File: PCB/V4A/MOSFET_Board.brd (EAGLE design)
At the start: 230 x 120 mm, 227 parts, among them IC1 7805T, IC2 7805T, Q101 SIRC10DP, Q102 SIRC10DP, Q103 BC817, Q104 BC817, Q105 SIRC10DP, Q106 SIRC10DP, Q107 BC817, Q108 BC807, Q109 BC817, Q110 BC807, Q111 IXTK102N65X2, Q112 IXTK102N65X2, Q301 BC807, Q302 BC807, Q303 BC807, Q304 BC807, Q305 BC807, Q306 BC807, Q307 BC807, Q308 BC807, U1 LM50, U101 AD420, U102 AD420, U103 LT1014I, U104 LT1014I, U105 AD620, U106 AD620, U107 AD620, U108 AD620, U109 LTC1865L, U110 LTC1865L, U111 LP2985-3.1, U2 LM50, U205 AD620, U208 LTC1865L, U3 LTC1865L, U301 HCPL-063N, U302 HCPL-063N, U303 HCPL-063N, U304 HCPL-063N, U4 MAX743, X1 GMSTBA4

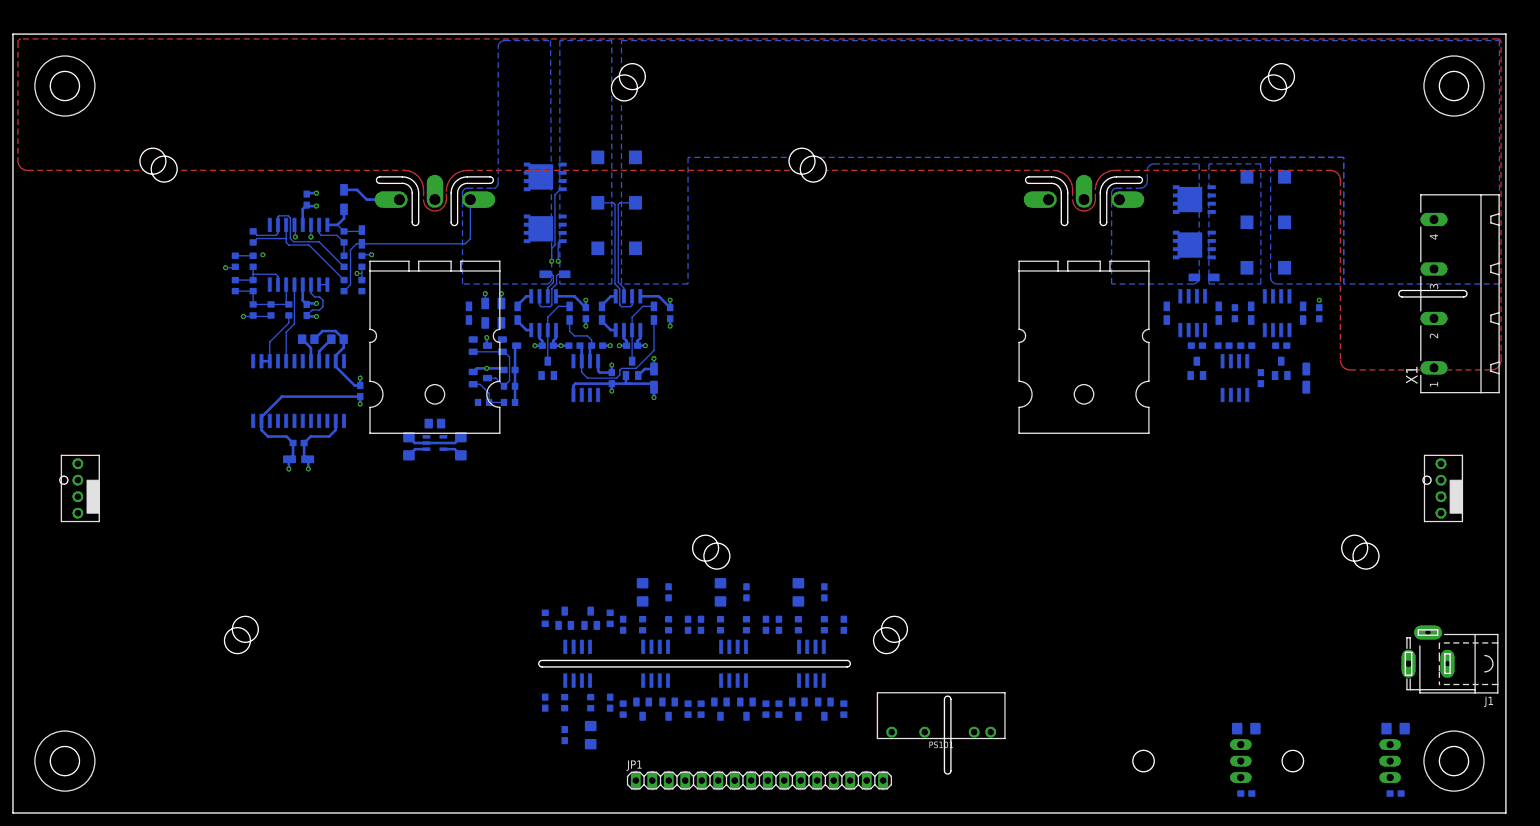
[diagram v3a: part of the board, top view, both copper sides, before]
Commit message: Added block diagram
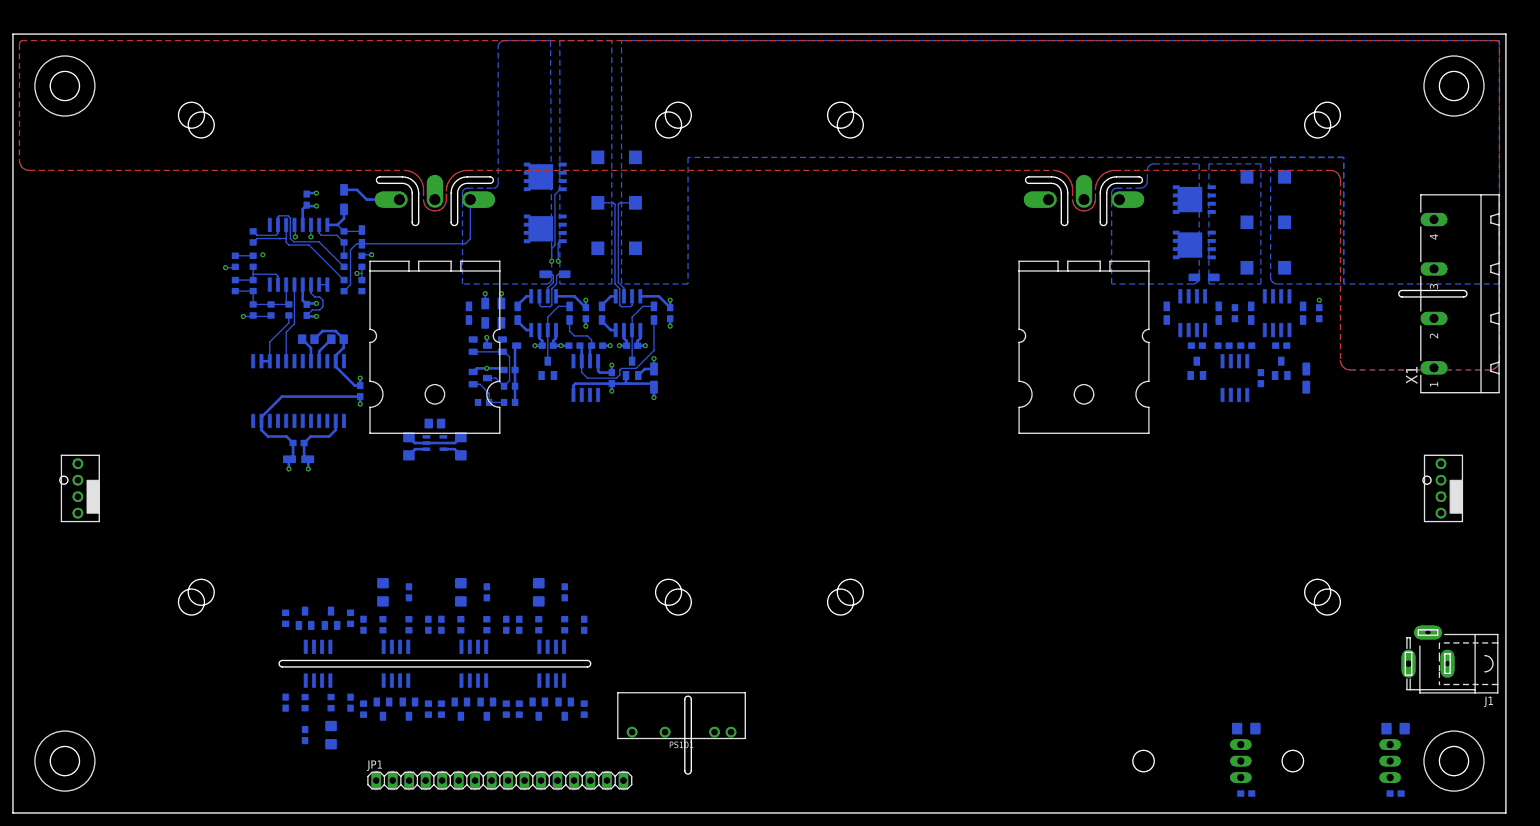
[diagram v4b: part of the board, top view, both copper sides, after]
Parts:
- moved C301 40.0 mm to (-54.0, -36.0)
- moved C302 40.0 mm to (-30.0, -36.0)
- moved C303 40.0 mm to (-58.0, -36.0)
- moved C304 40.0 mm to (-34.0, -36.0)
- moved C305 40.0 mm to (-51.0, -41.0)
- moved C306 40.0 mm to (-27.0, -41.0)
- moved C307 40.0 mm to (-61.0, -41.0)
- moved C308 40.0 mm to (-37.0, -41.0)
- moved C309 40.0 mm to (-42.0, -36.0)
- moved C310 40.0 mm to (-70.0, -58.0)
- moved C311 40.0 mm to (-46.0, -36.0)
- moved C312 40.0 mm to (-66.0, -58.0)
- moved C313 40.0 mm to (-39.0, -41.0)
- moved C314 40.0 mm to (-49.0, -41.0)
- moved C315 40.0 mm to (-73.0, -53.0)
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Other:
- outline, holes or cut-outs redrawn

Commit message: PCB layout, cleaned part list
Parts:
- removed C1, C11, C110, C3, C6: 1µ, passives:CT3216
- removed C10: 10µ, passives:CT6032
- removed C102, C104, C112, C114, C115, C118, C119, C120, C121, C17, C19: 0.1µ, passives:C1608
- removed C106, C108: 0.01µ, passives:C3216
- removed C12, C8: 10n, passives:C3216
- removed C13: 22µ, passives:CT6032
- removed C135: 1µ, passives:C3216
- removed C136: 10n, passives:C2012
- removed C137: 4µ7, passives:C3216
- removed C14, C15: 220µ, rcl:E3,5-10
- removed C16, C18: 0.33µ, passives:C3216
- removed C2, C7, C9: 0.1µ, passives:C3216
- removed C4, C5: 500p, passives:C1608
- removed Q103, Q107: BC817, transistors:SOT23
- removed Q108, Q302, Q303, Q305, Q306, Q307, Q308: BC807, transistors:SOT23
- removed R102, R104, R107, R108, R110, R112, R113, R114, R115, R116, R117, R118, R120, R122, R124, R126: 10k, passives:R1608
- removed R105, R106, R135: 100k, passives:R1608
- removed R128, R145: 2k15, passives:R2012W
- removed R129, R130: 100R, passives:R3216W
- removed R131, R137: 1k, passives:R1608
- removed R134, R140: 2R, passives:R3216W
- removed R3, R4: 100R, passives:R2012W
- removed R312, R313, R314, R315, R316: 350R, passives:R1608
- removed U1, U2: LM50, ic:SOT23W
- removed U102: AD420, ic:SO24W
- removed U104: LT1014I, ic:SO16W
- removed U105, U108: AD620, ic:SO8
- removed U111: LP2985-3.1, ic:SOT23-5L
- removed U3: LTC1865L, ic:SO8
- removed U4: MAX743, ic:SO16W
- added C202, C204, C212, C214, C401, C402, C403, C404, C417, C418, C419: 0.1µ, passives:C1608
- added C206, C208, C405, C406, C407, C408, C420, C421, C422: 0.01µ, passives:C3216
- added C210, C318, C319, C321, C326: 1µ, passives:CT3216
- added C317, C322, C323, C325, C327: 0.1µ, passives:C3216
- added C320: 150n, rcl:C050-030X075
- added C324: 500p, passives:C1608
- added C409, C410, C411, C412, C413, C414, C415, C416, C423, C424, C425, C426, C427, C428: 15p, passives:C1608
- added D303: BAT54S, diode:SOT23
- added Q203, Q207: BC817, transistors:SOT23
- added Q208, Q401, Q402, Q403, Q404, Q405, Q408, Q409, Q410, Q411, Q412, Q413, Q414: BC807, transistors:SOT23
- added R202, R204, R208, R210, R218, R220, R222, R224, R226: 10k, passives:R1608
- added R228, R247: 2k15, passives:R2012W
- added R229, R230: 100R, passives:R2012W
- added R231, R237: 1k, passives:R1608
- added R234, R240: 2R, passives:R3216W
- added R235: 100k, passives:R1608
- added R401, R402, R403, R404, R405, R406, R407, R408, R409, R410, R411, R412, R413, R414, R415, R416, R417, R418, R419, R420, R421, R422, R423, R424, R425, R426, R427, R428: 350R, passives:R1608
- added U202: AD420, ic:SO24W
- added U204: LT1014I, ic:SO16W
- added U305: AD620, ic:SO8
- added U306, U307: LTC1865L, ic:SO8
- added U401, U402, U403, U404, U405, U406, U407: HCPL-063N, ic:SO8
- C215, C219, C221: device passives:C3216 -> passives:C1608
- C218: value 500p -> 0.1µ
- C220: value 1µ -> 0.1µ; device passives:CT3216 -> passives:C1608
- C301, C302: value 0.1µ -> 0.33µ; device passives:C1608 -> passives:C3216
- C303: value 0.01µ -> 0.1µ
- C304: value 0.01µ -> 1µ; device passives:C3216 -> passives:CT3216
- C305, C307, C314: value 15p -> 10n; device passives:C1608 -> passives:C2012
- C306: value 15p -> 10µ; device passives:C1608 -> passives:CT6032
- C308: value 15p -> 0.1µ
- C310: value 0.1µ -> 22µ; device passives:C1608 -> passives:CT6032
- C311, C312: value 0.01µ -> 220µ; device passives:C3216 -> rcl:E3,5-10
- C313: value 15p -> 1µ; device passives:C1608 -> passives:C3216
- C315: value 15p -> 4µ7; device passives:C1608 -> passives:C3216
- C316: value 15p -> 0.1µ; device passives:C1608 -> passives:C3216
- L301, L302: device passives:SRN1060 -> passives:MSS1260
- R205, R206: value 2M -> 100k; device passives:R3216W -> passives:R1608
- R207, R212, R213: value 2M -> 10k; device passives:R3216W -> passives:R1608
- R214, R215: value 2k15 -> 10k; device passives:R2012W -> passives:R1608
- R216: value 100R -> 10k; device passives:R2012W -> passives:R1608
- R243, R245: value 3R3 -> 2R
- R301: value 350R -> 0R; device passives:R1608 -> passives:R3216W
- R302, R304, R305, R306, R307: value 350R -> 2M; device passives:R1608 -> passives:R3216W
- R303: value 350R -> 16R; device passives:R1608 -> rcl:0204/7
- R308, R309: value 350R -> 2k15; device passives:R1608 -> passives:R2012W
- R310: value 350R -> 100R; device passives:R1608 -> passives:R2012W
- R311: value 350R -> 10k
- U208: value LTC1865L -> AD620
- U301: value HCPL-063N -> MAX743; device ic:SO8 -> ic:SO16W
- U302: value HCPL-063N -> LP2985-3.1; device ic:SO8 -> ic:SOT23-5L
- U303, U304: value HCPL-063N -> LM50; device ic:SO8 -> ic:SOT23W
- moved C316 327.8 mm to (249.5, 46.0)
- moved U304 315.0 mm to (233.0, 46.0), turned to 0 degrees
- moved U303 304.5 mm to (246.0, 46.0)
- moved R207 285.4 mm to (-75.2, 7.50), flipped to the bottom, turned to 90 degrees
- moved R215 280.8 mm to (-78.0, 18.8), flipped to the bottom, turned to 90 degrees
- moved R213 279.3 mm to (-80.8, 11.2), flipped to the bottom, turned to 90 degrees
- moved R311 279.3 mm to (205.0, -13.0), flipped to the top, turned to 0 degrees
- moved R214 276.1 mm to (-78.0, 11.2), flipped to the bottom, turned to 90 degrees
- moved R310 271.1 mm to (218.0, -7.00), flipped to the top, turned to 0 degrees
- moved R205 270.6 mm to (-72.5, 7.50), flipped to the bottom, turned to 90 degrees
- moved R305 267.0 mm to (210.0, -1.00), flipped to the top, turned to 0 degrees
- moved R307 258.2 mm to (198.0, -7.00), flipped to the top, turned to 0 degrees
- moved R306 249.2 mm to (216.0, -1.00), flipped to the top, turned to 0 degrees
- moved R304 246.8 mm to (204.0, -1.00), flipped to the top, turned to 0 degrees
- moved R309 243.5 mm to (201.0, -13.0), flipped to the top, turned to 0 degrees
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- renumbered C101 to C201, C103 to C203, C105 to C205, C107 to C207, C109 to C209, C111 to C211, C113 to C213, C116 to C216, C117 to C217, C122 to C222, C123 to C223, C124 to C224, C125 to C225, C126 to C226, C127 to C227, C128 to C228, C129 to C229, C130 to C230, C131 to C231, C132 to C232, D101 to D201, D102 to D202, D103 to D203, D104 to D204, HS101 to HS201, HS102 to HS202, IC1 to IC301, IC2 to IC302, J1 to J301, JP1 to JP301, MOV201 to MOV301, MOV202 to MOV302, MOV203 to MOV303, MOV204 to MOV304, PS101 to PS301, Q101 to Q201, Q102 to Q202, Q104 to Q204, Q105 to Q205, Q106 to Q206, Q109 to Q209, Q110 to Q210, Q111 to Q211, Q112 to Q212, Q301 to Q407, Q304 to Q406, R1 to R249, R101 to R201, R103 to R203, R109 to R209, R111 to R211, R119 to R219, R121 to R221, R123 to R223, R125 to R225, R127 to R227, R132 to R232, R133 to R233, R136 to R236, R138 to R238, R139 to R239, R141 to R241, R142 to R242, R143 to R243, R144 to R245, R146 to R244, R147 to R248, R148 to R246, R149 to R251, R150 to R252, R151 to R253, R152 to R254, R153 to R255, R154 to R256, R155 to R257, R156 to R258, R2 to R250, U$2 to J302, U$3 to J303, U101 to U201, U103 to U203, U106 to U206, U107 to U207, U109 to U209, U110 to U210, X1 to X301
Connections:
- net CLR_DAC renamed CONV_C2_I
- net SS_C renamed CONV_V_I
- removed net BYP_ISO: C306.1, R131.1, R233.1, R306.1, U302.7
- removed net CLR_DAC_ISO: C305.1, R305.1, U301.7
- removed net FLT_DAC_ISO: Q308.1
- removed net MISO_ISO: Q307.1
- removed net MOSI_ISO: C314.1, R314.1, U303.6
- removed net SCK_ISO: C313.1, R313.1, U303.7
- removed net SS_C_ISO: C308.1, R308.1, U302.6
- removed net SS_DAC: Q303.1
- removed net SS_DAC_ISO: C307.1, R307.1, U301.6
- removed net SS_TEMP_I: U3.1
- removed net SS_V_I: U208.1
- removed net T1_OUT: C1.+, R3.1, U1.2
- removed net T2_OUT: C3.+, R4.1, U2.2
- new net BYP_I: Q401.1
- new net CLR_DAC1_I: Q410.1
- new net CLR_DAC2_I: Q413.1
- new net CONV_C1_I: Q403.1
- new net CONV_TEMP: C410.1, R410.1, U306.1, U402.7
- new net CONV_TEMP_I: Q402.1
- new net CONV_V: C414.1, R414.1, U307.1, U402.6
- new net FAN1_PWM_I: Q409.1
- new net FAN2_PWM_I: Q412.1
- new net FLT_DAC_I: C428.1, R428.1, U407.6
- new net LATCH_DAC_I: Q405.1
- new net N$40: Q409.2, R417.1, U405.1
- new net N$46: Q412.2, R420.1, U405.4
- new net N$47: Q401.2, R401.1, U401.1
- new net N$48: Q405.2, R405.1, U401.4
- new net N$58: Q410.2, R418.1, U406.1
- new net N$59: Q413.2, R421.1, U406.4
- new net N$61: C320.1, R303.1
- new net VREF_MAX743: C306.+, U301.6
- net +12V: now also C206.1, C208.1, C214.1, C215.1, C301.1, C302.1, Q207.3, R235.2, R237.2, U202.23; no longer C106.1, C108.1, C114.1, C115.1, C16.1, C18.1, Q107.3, R135.2, R137.2, U102.23
- net +15V: now also C202.1, C218.1, C219.1, C220.1, C311.+, C323.1, U204.4, U208.7, U301.16, U305.7; no longer C102.1, C118.1, C119.1, C120.1, C14.+, C215.1, U104.4, U105.7, U108.7, U4.16
- net +3V3: now also C315.1, C321.+, C322.1, C326.+, C327.1, D303.2, R412.2, R413.2, R414.2, R416.2, R426.2, R427.2, U302.5, U306.8, U307.8; no longer C137.1, C220.+, C221.1, C6.+, C7.1, R308.2, R313.2, R314.2, U111.5, U208.8, U3.8
- net +5V: now also C210.+, C212.1, C303.2, C308.1, C310.+, C316.1, C317.1, C401.1, C402.1, C403.1, C404.1, C405.1, C406.1, C407.1, C408.1, C417.1, C418.1, C420.1, C421.1, R409.2, R410.2, R411.2, R415.2, R419.2, R422.2, R423.2, R424.2, U202.2, U301.12, U301.13, U301.3, U301.4, U301.5, U303.1, U304.1, U401.8, U402.8, U403.8, U404.8, U405.8, U406.8; no longer C110.+, C112.1, C13.+, C17.1, C19.1, C2.1, C301.1, C302.1, C303.1, C304.1, C311.1, C9.2, R301.2, R302.2, R303.2, R304.2, R305.2, R306.2, R307.2, R309.2, R310.2, R311.2, R312.2, R315.2, R316.2, U1.1, U102.2, U2.1, U301.8, U302.8, U303.8, U304.8, U4.12, U4.13, U4.3, U4.4, U4.5
- net +5V_I: now also C419.1, C422.1, R401.2, R402.2, R403.2, R404.2, R405.2, R406.2, R407.2, R408.2, R417.2, R418.2, R420.2, R421.2, R425.2, R428.2, U407.8; no longer C310.1, C312.1
- net -15V: now also C204.1, C221.1, C312.-, C325.1, U204.13, U208.4, U301.9, U305.4; no longer C104.1, C121.1, C15.-, C219.1, U104.13, U105.4, U108.4, U4.9
- net BYP: now also C409.1, R231.1, R233.1, R409.1, U401.7; no longer Q302.1
- net BYP2: now also Q207.2, Q208.2, R234.1, R240.1, R247.2; no longer Q107.2, Q108.2, R134.1, R140.1, R145.2
- net BYP2G1: now also R234.2; no longer R134.2
- net BYP2G2: now also R240.2; no longer R140.2
- net CLR_DAC1: now also C424.1, R424.1, U406.7
- net CLR_DAC2: now also C427.1, R427.1, U202.6, U406.6; no longer U102.6
- net CONV_C1: now also C411.1, R411.1, U403.7
- net CONV_C2: now also C415.1, R415.1, U403.6
- net CSEN_H1: now also U205.3; no longer U105.3
- net CSEN_H2: now also R247.1, U208.2; no longer R145.1, U108.2
- net CSEN_L2: now also R202.1, R228.1, U208.3; no longer R102.1, R128.1, U108.3
- net DAC_VOUT1: now also U202.17, U204.5; no longer U102.17, U104.5
- net DUT+: now also R303.2
- net DUT-: now also C320.2, R204.1, R301.2, U205.2; no longer R104.1, U105.2
- net FAN1_PWM: now also C423.1, R423.1, U405.7
- net FAN2_PWM: now also C426.1, R426.1, U405.6
- net FLT_DAC: now also Q414.1, U202.3; no longer C316.1, R316.1, U102.3, U304.6
- net GND: now also C202.2, C204.2, C210.-, C212.2, C214.2, C220.2, C303.1, C304.-, C305.1, C306.-, C310.-, C311.-, C312.+, C315.2, C316.2, C317.2, C318.-, C319.-, C321.-, C322.2, C323.2, C324.2, C325.2, C326.-, C327.2, C401.2, C402.2, C403.2, C404.2, C405.2, C406.2, C407.2, C408.2, C409.2, C410.2, C411.2, C412.2, C413.2, C414.2, C415.2, C416.2, C417.2, C418.2, C420.2, C421.2, C423.2, C424.2, C426.2, C427.2, D303.1, Q203.2, Q208.3, Q411.3, Q414.3, R207.1, R208.1, R210.1, R212.1, R224.1, R301.1, R308.1, R311.1, U202.11, U202.4, U202.5, U204.3, U208.5, U301.11, U301.14, U301.2, U302.2, U303.3, U305.5, U306.4, U307.4, U401.5, U402.5, U403.5, U404.5, U405.5, U406.5, U407.2, U407.3; no longer C1.-, C10.-, C102.2, C104.2, C11.-, C110.-, C112.2, C114.2, C115.2, C118.2, C119.2, C12.2, C120.2, C121.2, C13.-, C135.2, C136.2, C137.2, C14.-, C15.+, C16.2, C17.2, C18.2, C19.2, C2.2, C220.-, C3.-, C303.2, C304.2, C305.2, C306.2, C311.2, C4.2, C5.2, C6.-, C7.2, C8.1, C9.1, Q103.2, Q108.3, Q307.3, Q308.3, R107.1, R108.1, R110.1, R112.1, R124.1, R214.1, R217.1, U1.3, U102.11, U102.4, U102.5, U104.3, U105.5, U108.5, U111.2, U2.3, U208.4, U3.4, U301.5, U302.5, U303.5, U304.2, U4.11, U4.14, U4.2
- net GNDI: now also C419.2, C422.2, C425.2, C428.2, Q401.3, Q402.3, Q403.3, Q404.3, Q405.3, Q408.3, Q409.3, Q410.3, Q412.3, Q413.3, U401.2, U401.3, U402.2, U402.3, U403.2, U403.3, U404.2, U404.3, U405.2, U405.3, U406.2, U406.3, U407.5; no longer C310.2, C312.2, C315.2, C316.2, Q302.3, Q303.3, Q305.3, Q306.3, U301.2, U301.3, U302.2, U302.3, U303.2, U303.3, U304.5
- net LATCH_DAC: now also C413.1, R413.1, U202.7, U401.6; no longer U102.7
- net LGATE_1: now also R229.2; no longer R129.2
- net LGATE_2: now also R230.2; no longer R130.2
- net MISO: now also Q411.1, U306.6, U307.6; no longer C315.1, R315.1, U304.7
- net MISO_I: now also C425.1, R425.1, U407.7; no longer U208.6, U3.6
- net MOSI: now also C416.1, R416.1, U306.5, U307.5, U404.6; no longer Q306.1
- net MOSI_I: now also Q408.1; no longer U208.5, U3.5
- net N$10: now also C314.1, U302.4; no longer C136.1, U111.4
- net N$11: now also R213.2, R214.2; no longer R113.2, R114.2
- net N$12: now also R205.2, R207.2, R213.1, R214.1; no longer R105.2, R107.2, R113.1, R114.1
- net N$13: now also R215.2; no longer R115.2
- net N$14: now also R215.1; no longer R115.1
- net N$17: now also Q411.2, R419.1, U407.1; no longer Q307.2, R311.1, U304.1
- net N$18: now also Q414.2, R422.1, U407.4; no longer Q308.2, R312.1, U304.4
- net N$19: now also Q404.2, R404.1, U404.1; no longer Q305.2, R309.1, U303.1
- net N$20: now also Q408.2, R408.1, U404.4; no longer Q306.2, R310.1, U303.4
- net N$21: now also Q402.2, R402.1, U402.1; no longer Q302.2, R302.1, U302.1
- net N$22: now also R406.1, U402.4; no longer R304.1, U302.4
- net N$23: now also R310.1, U305.6; no longer R216.1, U205.6
- net N$24: now also R306.1, R307.2; no longer R212.1, R213.2
- net N$25: now also Q203.3, Q207.1, Q208.1, R237.1; no longer Q103.3, Q107.1, Q108.1, R137.1
- net N$26: now also R304.2, R306.2; no longer R206.2, R212.2
- net N$27: now also R304.1, R305.2; no longer R206.1, R207.2
- net N$29: now also R307.1, R308.2, U305.3; no longer R213.1, R214.2, U205.3
- net N$30: now also C324.1, D303.3, R310.2, U307.2; no longer C218.1, R216.2, U208.2
- net N$31: now also Q203.1, R231.2, R235.1; no longer Q103.1, R131.2, R135.1
- net N$33: now also R302.2, R305.1; no longer R205.2, R207.1
- net N$34: now also C307.1, U301.8; no longer C12.1, U4.8
- net N$35: now also C304.+, U301.7; no longer C11.+, U4.7
- net N$37: now also C305.2, U301.1; no longer C8.2, U4.1
- net N$38: now also U301.15; no longer U4.15
- net N$39: now also U301.10; no longer U4.10
- net N$41: now also C206.2, U202.21; no longer C106.2, U102.21
- net N$42: now also C208.2, U202.20; no longer C108.2, U102.20
- net N$43: now also R206.2, R208.2, R212.2, R216.1, R217.1, U204.6; no longer R106.2, R108.2, R112.2, R116.1, R117.1, U104.6
- net N$44: now also R218.2, R222.1, U204.10; no longer R118.2, R122.1, U104.10
- net N$45: now also R311.2, U307.3; no longer R217.2, U208.3
- net N$49: now also R202.2, R218.1, U204.11; no longer R102.2, R118.1, U104.11
- net N$50: now also R204.2, R210.2, U204.12; no longer R104.2, R110.2, U104.12
- net N$51: now also R222.2, R226.1, U204.15; no longer R122.2, R126.1, U104.15
- net N$52: now also R226.2, R228.2, R230.1, U204.16; no longer R126.2, R128.2, R130.1, U104.16
- net N$53: now also R220.2, R224.2, U204.14; no longer R120.2, R124.2, U104.14
- net N$54: now also R216.2, R217.2, R220.1, U204.7; no longer R116.2, R117.2, R120.1, U104.7
- net N$55: now also U204.1, U204.2; no longer U104.1, U104.2
- net N$57: now also U208.6; no longer U108.6
- net N$6: now also R229.1; no longer R129.1
- net N$7: now also U205.6; no longer U105.6
- net N$76: now also Q403.2, R403.1, U403.1; no longer Q407.2, R301.1, U301.1
- net N$77: now also Q407.2, R407.1, U403.4; no longer Q303.2, R303.1, U301.4
- net RG1_H6: now also R309.2, U305.1; no longer R215.2, U205.1
- net RG1_L2: now also U208.1; no longer U108.1
- net RG1_L3: now also U205.1; no longer U105.1
- net RG2_H6: now also R309.1, U305.8; no longer R215.1, U205.8
- net RG2_L2: now also U208.8; no longer U108.8
- net RG2_L3: now also U205.8; no longer U105.8
- net SCK: now also C412.1, R412.1, U202.8, U306.7, U307.7, U404.7; no longer Q305.1, U102.8
- net SCK_I: now also Q404.1; no longer U208.7, U3.7
- net SDO_DAC1: now also U202.9; no longer U102.9
- net SDO_DAC2: now also U202.10; no longer U102.10
- net TEMP1: now also C318.+, U303.2, U306.2; no longer C4.1, R3.2, U3.2
- net TEMP2: now also C319.+, U304.2, U306.3; no longer C5.1, R4.2, U3.3
- net VREF1: now also C313.1, R205.1, U302.1, U302.3; no longer C135.1, R105.1, U111.1, U111.3
- net VREF2: now also R206.1, U202.14, U202.15; no longer C10.+, R106.1, U102.14, U102.15, U4.6
- net VSENSE+: now also R302.1; no longer R205.1
- net VSENSE-: now also U305.2; no longer U205.2
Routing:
- net GND: vias 16 -> 17
